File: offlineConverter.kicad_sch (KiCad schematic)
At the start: 71 parts, among them IC1 NCP12510ASN65T1G, IC2 SFH6156-3, Q1 STD3NK80ZT4, Q2 BAT847B, T1 750343466, U2 TL432DBZ

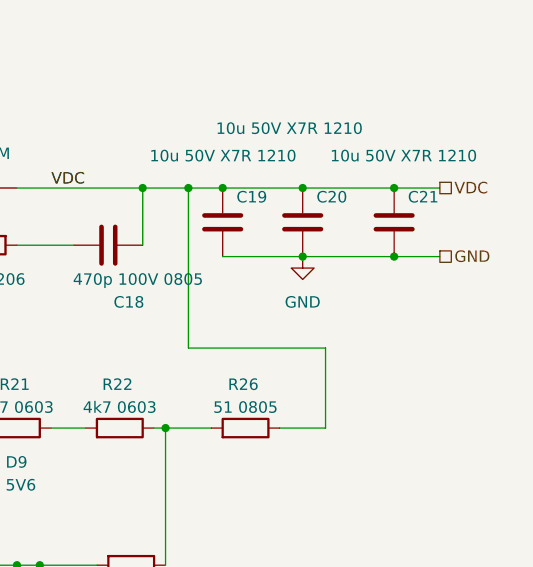
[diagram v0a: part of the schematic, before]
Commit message: update of schematic
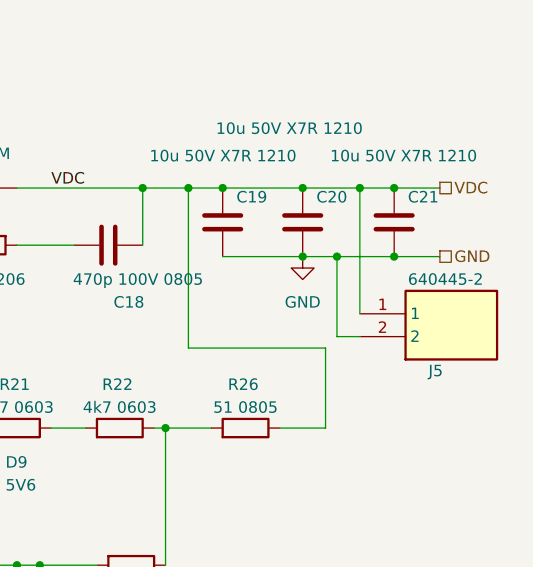
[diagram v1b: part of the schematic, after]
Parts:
- added J5: 640445-2, 6404452, symbol Hansmann:640445-2
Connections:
- net GND: now also J5.2
- net VDC: now also J5.1
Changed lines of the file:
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@@
 	)
 	(junction
+		(at 269.24 118.11)
+		(diameter 0)
+		(color 0 0 0 0)
+	)
+	(junction
 		(at 100.33 140.97)
 		(diameter 0)
@@
 	)
 	(junction
+		(at 266.7 125.73)
+		(diameter 0)
+		(color 0 0 0 0)
+	)
+	(junction
 		(at 78.74 140.97)
 		(diameter 0)
@@
 	(wire
 		(pts
+			(xy 269.24 132.08) (xy 269.24 118.11)
+		)
+		(stroke
+			(width 0)
+			(type default)
+		)
+	)
+	(wire
+		(pts
 			(xy 76.2 132.08) (xy 76.2 123.19)
 		)
@@
 	(wire
 		(pts
+			(xy 269.24 118.11) (xy 273.05 118.11)
+		)
+		(stroke
+			(width 0)
+			(type default)
+		)
+	)
+	(wire
+		(pts
 			(xy 54.61 105.41) (xy 62.23 105.41)
 		)
@@
 	(wire
 		(pts
+			(xy 266.7 134.62) (xy 269.24 134.62)
+		)
+		(stroke
+			(width 0)
+			(type default)
+		)
+	)
+	(wire
+		(pts
 			(xy 46.99 113.03) (xy 30.48 113.03)
 		)
@@
 	(wire
 		(pts
+			(xy 266.7 125.73) (xy 266.7 134.62)
+		)
+		(stroke
+			(width 0)
+			(type default)
+		)
+	)
+	(wire
+		(pts
 			(xy 146.05 59.69) (xy 153.67 59.69)
 		)
@@
 	(wire
 		(pts
-			(xy 262.89 118.11) (xy 273.05 118.11)
+			(xy 262.89 118.11) (xy 269.24 118.11)
+		)
+		(stroke
+			(width 0)
+			(type default)
+		)
+	)
+	(wire
+		(pts
+			(xy 266.7 125.73) (xy 273.05 125.73)
 		)
 		(stroke
@@
 	(wire
 		(pts
-			(xy 262.89 125.73) (xy 273.05 125.73)
+			(xy 262.89 125.73) (xy 266.7 125.73)
 		)
 		(stroke
@@
 		(polyline
 			(pts
-				(xy 165.1 110.49) (xy 165.1 77.47) (xy 24.13 77.47) (xy 24.13 109.22) (xy 36.83 109.22) (xy 36.83 85.09)
-				(xy 87.63 85.09) (xy 87.63 110.49) (xy 92.71 110.49)
+				(xy 53.34 29.21) (xy 53.34 73.66) (xy 180.34 73.66) (xy 180.34 54.61) (xy 223.52 54.61) (xy 223.52 29.21)
 			)
 			(stroke
@@
 		(polyline
 			(pts
-				(xy 53.34 29.21) (xy 53.34 73.66) (xy 180.34 73.66) (xy 180.34 54.61) (xy 223.52 54.61) (xy 223.52 29.21)
+				(xy 165.1 110.49) (xy 165.1 77.47) (xy 24.13 77.47) (xy 24.13 109.22) (xy 36.83 109.22) (xy 36.83 85.09)
+				(xy 87.63 85.09) (xy 87.63 110.49) (xy 92.71 110.49)
 			)
 			(stroke
@@
 					(unit 1)
 				)
+			)
+		)
+	)
+	(symbol
+		(lib_id "Hansmann:640445-2")
+		(at 269.24 134.62 0)
+		(mirror x)
+		(unit 1)
+		(exclude_from_sim no)
+		(in_bom yes)
+		(on_board yes)
+		(dnp no)
+		(property "Reference" "J5"
+			(at 276.86 138.43 0)
+			(effects
+				(font
+					(size 1.27 1.27)
+				)
+				(justify left)
+			)
+		)
+		(property "Value" "640445-2"
+			(at 274.574 128.27 0)
+			(effects
+				(font
+					(size 1.27 1.27)
+				)
+				(justify left)
+			)
+		)
+		(property "Footprint" "6404452"
+			(at 285.75 39.7 0)
+			(effects
+				(font
+					(size 1.27 1.27)
+				)
+				(justify left top)
+				(hide yes)
+			)
+		)
+		(property "Datasheet" "https://componentsearchengine.com/Datasheets/2/640445-2.pdf"
+			(at 285.75 -60.3 0)
+			(effects
+				(font
+					(size 1.27 1.27)
+				)
+				(justify left top)
+				(hide yes)
+			)
+		)
+		(property "Description" "Configuration Features: PCB Mount Orientation Vertical | Number of Power Positions 2 | Number of Positions 2 | Number of Rows 1 | Contact Features: Contact Mating Area Plating Material Thickness 2.54 MICM | Contact Type Pin | Contact Layout Inline | Mating Post Length 10.16 MM | Mating Post Length .4 INCH | Contact Mating Area Plating Material Tin | PCB Contact Termination Area Plating Material Tin | Contact Mating Area Plating Material Thickness 100 MICIN | Contact Retention Within Housing Without | Contac"
+			(at 269.24 134.62 0)
+			(effects
+				(font
+					(size 1.27 1.27)
+				)
+				(hide yes)
+			)
+		)
+		(property "Height" "11.049"
+			(at 285.75 -260.3 0)
+			(effects
+				(font
+					(size 1.27 1.27)
+				)
+				(justify left top)
+				(hide yes)
+			)
+		)
+		(property "Mouser Part Number" "5716404452"
+			(at 285.75 -360.3 0)
+			(effects
+				(font
+					(size 1.27 1.27)
+				)
+				(justify left top)
+				(hide yes)
+			)
+		)
+		(property "Mouser Price/Stock" "https://www.mouser.co.uk/ProductDetail/TE-Connectivity-AMP/640445-2?qs=P8zzrVhehau7EdfErby3cQ%3D%3D"
+			(at 285.75 -460.3 0)
+			(effects
+				(font
+					(size 1.27 1.27)
+				)
+				(justify left top)
+				(hide yes)
+			)
+		)
+		(property "Manufacturer_Name" "TE Connectivity"
+			(at 285.75 -560.3 0)
+			(effects
+				(font
+					(size 1.27 1.27)
+				)
+				(justify left top)
+				(hide yes)
+			)
+		)
+		(property "Manufacturer_Part_Number" "640445-2"
+			(at 285.75 -660.3 0)
+			(effects
+				(font
+					(size 1.27 1.27)
+				)
+				(justify left top)
+				(hide yes)
+			)
+		)
+		(pin "2"
+		)
+		(pin "1"
+		)
+		(instances
+			(project "OSLUV"
+				(path "/c6e900e0-9399-44f0-8089-9dd7b8ffe54c/a8d7965e-5268-4c95-93ca-40f8dbbf325c"
+					(reference "J5")
+					(unit 1)
+				)

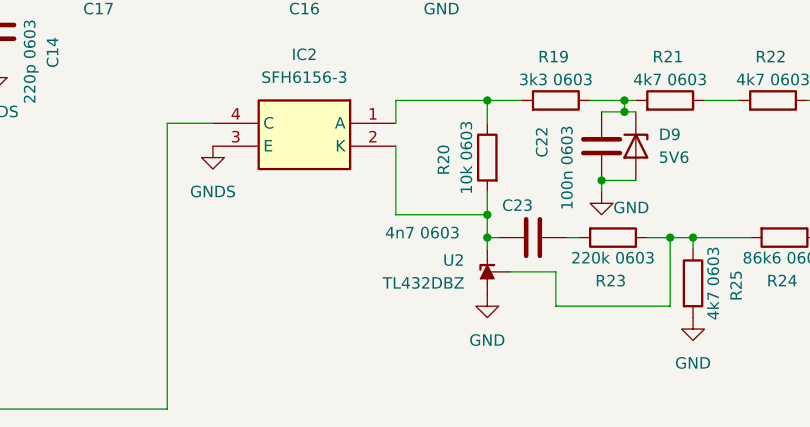
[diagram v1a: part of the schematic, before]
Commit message: schematic done, not placed
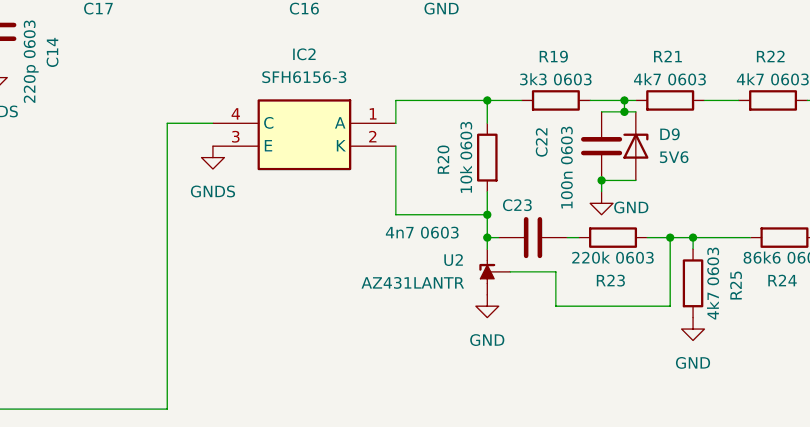
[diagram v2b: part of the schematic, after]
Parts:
- U2: value TL432DBZ -> AZ431LANTR
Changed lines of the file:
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@@
+		(polyline
+			(pts
+				(xy 21.59 29.21) (xy 21.59 73.66) (xy 52.07 73.66) (xy 52.07 33.655) (xy 52.07 29.21)
+			)
+			(stroke
+				(width 0)
+				(type dash)
+			)
+			(fill
+				(type none)
+			)
+		)
+	)
+	(rule_area
 		(polyline
 			(pts
@@
 		)
 	)
-	(rule_area
-		(polyline
-			(pts
-				(xy 21.59 29.21) (xy 21.59 73.66) (xy 52.07 73.66) (xy 52.07 33.655) (xy 52.07 29.21)
-			)
-			(stroke
-				(width 0)
-				(type dash)
-			)
-			(fill
-				(type none)
-			)
-		)
-	)
 	(netclass_flag ""
 		(length 2.54)
@@
 			)
 		)
-		(property "Value" "TL432DBZ"
+		(property "Value" "AZ431LANTR"
 			(at 208.28 165.0999 90)
 			(effects
